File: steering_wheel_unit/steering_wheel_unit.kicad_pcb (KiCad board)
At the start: 2 copper layers, 90 x 70 mm, 130 parts, among them IC2 LM76202QPWPRQ1, J1 MAIN_CONNECTOR, J10 MODE2_SOCKET, J11 FUEL_CELL_SOCKET, J12 USB_C_Vertical, J13 Additional goldpins, J14 LCD_SOCKET, J15 JTAG_SOCKET, J16 Additional goldpins from MCU, J3 HALF_GAS_SOCKET, J4 MODE1_SOCKET, J5 FULL_GAS_SOCKET, J6 SPEED_RESET_SOCKET, J7 HORN_SOCKET, J8 SC_CLOSE_SOCKET, J9 SUPPLY_SOCKET, SW1 TL3305BF100QG, SW2 TL3305BF100QG, SW3 TL3305BF100QG, U1 STM32G491CCTx, U2 USBLC6-2P6, U3 SN65HVD232, U4 TPS62933, X1 32k768, X2 24M

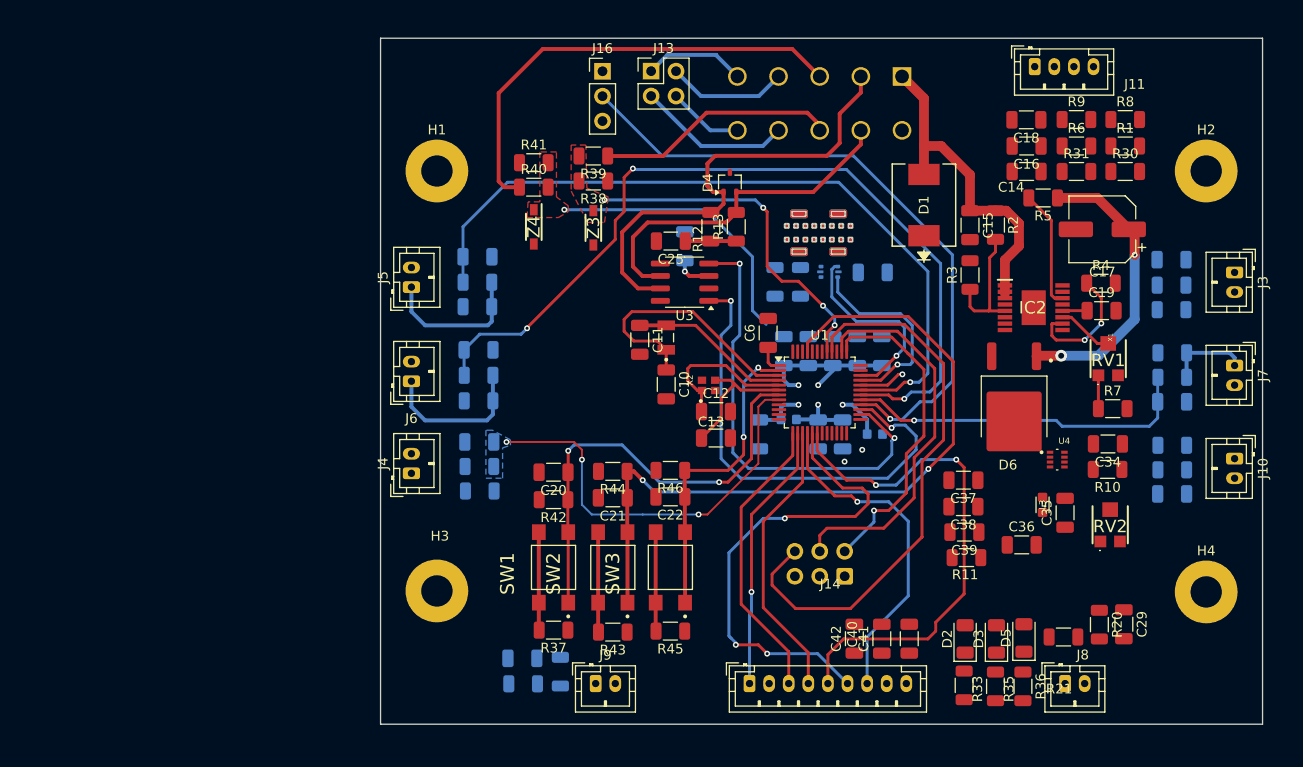
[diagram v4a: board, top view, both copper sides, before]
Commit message: Add zones for gnd and power
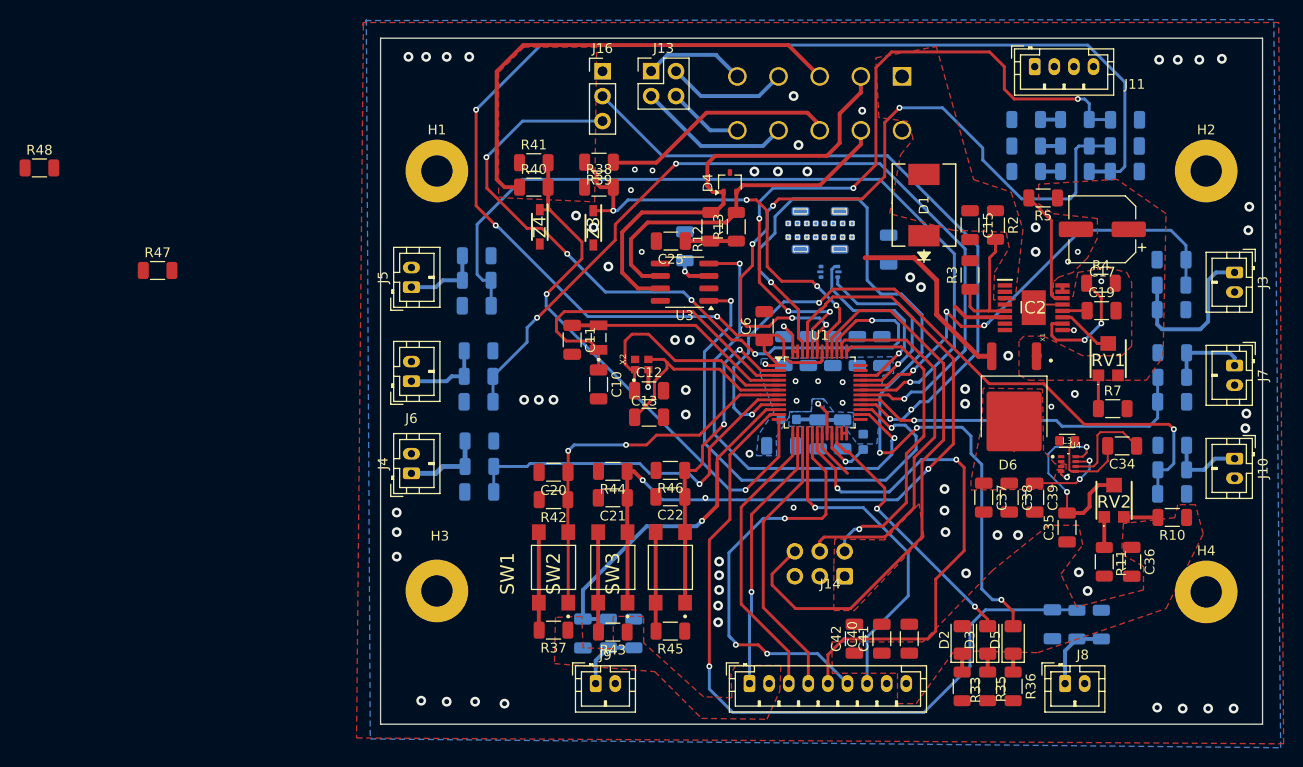
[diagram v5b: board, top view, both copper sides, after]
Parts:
- removed J12: USB_C_Vertical, Lib:CUI_UJ20-C-V-C-3-SMT-TR
- removed R32, R34: 5K1, Resistor_SMD:R_1206_3216Metric
- added J2: UJ20-C-V-C-3-SMT-TR, Lib:CUI_UJ20-C-V-C-2-SMT-TR, B.Cu at (186.7, 96.2)
- added R47: 5K1, Resistor_SMD:R_1206_3216Metric, F.Cu at (119.1, 100.3)
- added R48: 5K1, Resistor_SMD:R_1206_3216Metric, F.Cu at (107.0, 89.8)
- C14, C16, C18, C29, R1, R20, R21, R30, R31, R6, R8, R9: moved to B.Cu
- moved R11 14.1 mm to (215.7, 130.0), turned to -90 degrees
- moved C36 11.4 mm to (218.5, 130.0), turned to -90 degrees
- moved R1 10.1 mm to (207.7, 87.6), turned to 180 degrees
- moved R30 10.1 mm to (207.7, 90.2), turned to 180 degrees
- moved R8 10.1 mm to (207.7, 84.9), turned to 180 degrees
- moved R23 10.1 mm to (165.1, 137.3), turned to -90 degrees
- moved C18 10.1 mm to (217.8, 84.9), turned to 0 degrees
- moved C14 10.0 mm to (217.8, 90.2), turned to 0 degrees
- moved C16 10.0 mm to (217.8, 87.6), turned to 0 degrees
- moved R27 8.45 mm to (167.7, 137.3)
- moved R10 8.22 mm to (222.6, 125.5)
- moved C39 7.99 mm to (208.6, 123.5), turned to -90 degrees
- moved C29 7.29 mm to (210.4, 136.4)
- moved C12 7.15 mm to (169.3, 112.6)
- moved C13 7.15 mm to (169.3, 115.3)
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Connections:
- net Net-(U1-VREF+) renamed /MCU/VREF
- net Net-(U4-VIN) renamed /POWER/VIN
- U1 pad 22: /MCU/MCU_LED -> /IO/MCU_LED
- U1 pad 46: /MCU/CAN_LED -> /IO/CAN_LED
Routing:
- net /IO/FUEL_CELL_RACE_BUTTON_MCU: track 0.00 -> 136.6 mm, vias 0 -> 3
- net /IO/CAN_LED: track 0.00 -> 89.6 mm, vias 0 -> 4
- net /IO/FUEL_CELL_PREPARE_TO_RAC_BUTTON_MCU: track 0.00 -> 77.4 mm, vias 0 -> 5
- net /IO/SC_CLOSE_BUTTON_MCU: track 0.00 -> 76.8 mm, vias 0 -> 1
- net /MCU/GPIO_PB15: track 0.00 -> 76.3 mm, vias 0 -> 5
- net /IO/FUEL_CELL_OFF_BUTTON_MCU: track 0.00 -> 74.7 mm, vias 0 -> 5
- net /IO/MODE2_BUTTON_MCU: track 0.00 -> 72.5 mm, vias 0 -> 3
- net /IO/HALF_GAS_BUTTON_MCU: track 4.73 -> 47.9 mm, vias 1 -> 3
- net /IO/SUPPLY_BUTTON_MCU: track 0.00 -> 36.0 mm, vias 0 -> 1
- net +12V: track 33.9 -> 0.16 mm
- net /POWER/Vreg: track 29.6 -> 0.72 mm, vias 2 -> 0
- net /IO/MCU_LED: track 0.00 -> 26.9 mm, vias 0 -> 2
- net /MCU/PA4: track 28.7 -> 55.3 mm, vias 1 -> 2
- net GND: track 0.00 -> 21.9 mm, vias 2 -> 74
- net Net-(U4-FB): track 0.00 -> 19.7 mm, vias 0 -> 2
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- added copper zone on F.Cu, net +12V
- added copper zone on B.Cu, net +3.3V
- added copper zone on F.Cu, net +3.3V
- added copper zone on B.Cu, net /MCU/VREF
- added copper zone on F.Cu, net /POWER/VIN
- added copper zone on F.Cu, net /POWER/Vreg
- added copper zone on B.Cu, net GND
- added copper zone on F.Cu, net GND
- removed copper zone on B.Cu, net /IO/MODE1_BUTTON_MCU
- removed copper zone on F.Cu, net /MCU/PA4
- removed copper zone on F.Cu, net /MCU/PB4

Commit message: Add some routing changes
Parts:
- R47, R48: moved to B.Cu
- moved R48 87.1 mm to (193.5, 100.1), turned to -90 degrees
- moved R47 77.1 mm to (196.2, 100.1), turned to -90 degrees
- moved C23 18.0 mm to (175.7, 97.9), turned to 90 degrees
- moved C18 16.9 mm to (200.9, 84.1), turned to -90 degrees
- moved R9 9.21 mm to (203.5, 84.1), turned to 90 degrees
- moved R1 9.05 mm to (216.2, 84.3), turned to -90 degrees
- moved C16 7.62 mm to (210.9, 84.3), turned to -90 degrees
- moved C26 5.40 mm to (222.7, 104.6), turned to 0 degrees
- moved R14 4.60 mm to (222.7, 99.7), turned to 180 degrees
- moved R6 3.39 mm to (213.6, 84.3), turned to -90 degrees
- moved R30 3.02 mm to (210.8, 90.3), turned to -90 degrees
- moved U2 2.92 mm to (184.7, 100.5), turned to 180 degrees
- moved R8 1.78 mm to (206.1, 84.1), turned to -90 degrees
- moved C14 1.59 mm to (216.2, 90.3), turned to -90 degrees
- moved C34 0.90 mm to (217.5, 119.1)
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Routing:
- net +3.3V: track 8.71 -> 300.3 mm, vias 7 -> 16
- net /FUEL_CELL_RACE_MODE: track 2.05 -> 26.9 mm
- net /IO/FUEL_CELL_OFF_BUTTON_MCU: track 74.7 -> 62.6 mm
- net /HALF_GAS: track 17.0 -> 7.67 mm
- net /FUEL_CELL_PREPARE_TO_RACE: track 2.05 -> 11.3 mm
- net /FUEL_CELL_OFF: track 2.05 -> 9.64 mm
- net /IO/HALF_GAS_BUTTON_MCU: track 47.9 -> 40.4 mm
- net /LCD_CS: track 34.4 -> 40.9 mm, vias 1 -> 3
- net /IO/FUEL_CELL_RACE_BUTTON_MCU: track 136.6 -> 142.9 mm
- net /MCU/PA4: track 55.3 -> 61.6 mm
- net /MCU/USB_DN: track 19.7 -> 25.1 mm
- net /IO/FUEL_CELL_PREPARE_TO_RAC_BUTTON_MCU: track 77.4 -> 73.2 mm
- net /IO/FULL_GAS_BUTTON_MCU: track 84.0 -> 86.7 mm
- net /IO/MODE2_BUTTON_MCU: track 72.5 -> 75.0 mm
- net /SC_CLOSE: track 7.54 -> 10.0 mm
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
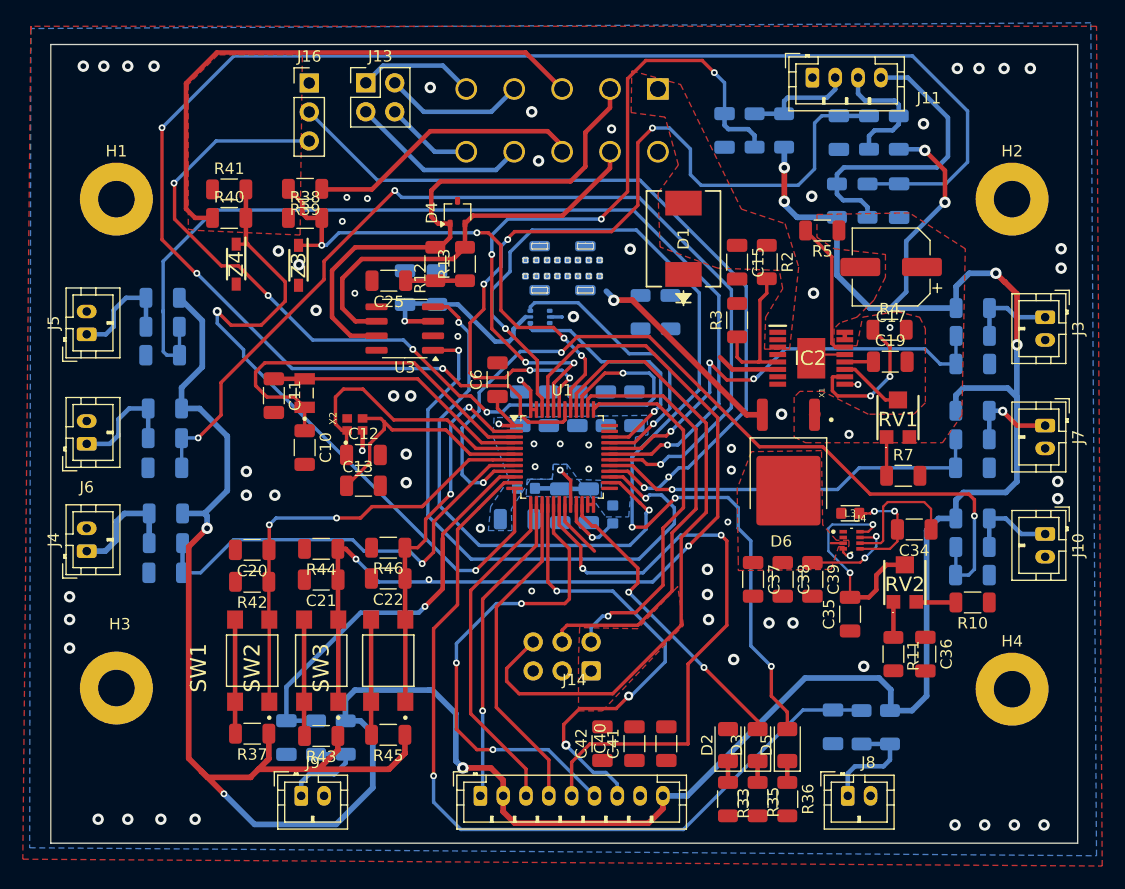
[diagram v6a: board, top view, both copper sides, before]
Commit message: Edit tracks and add captions of elements
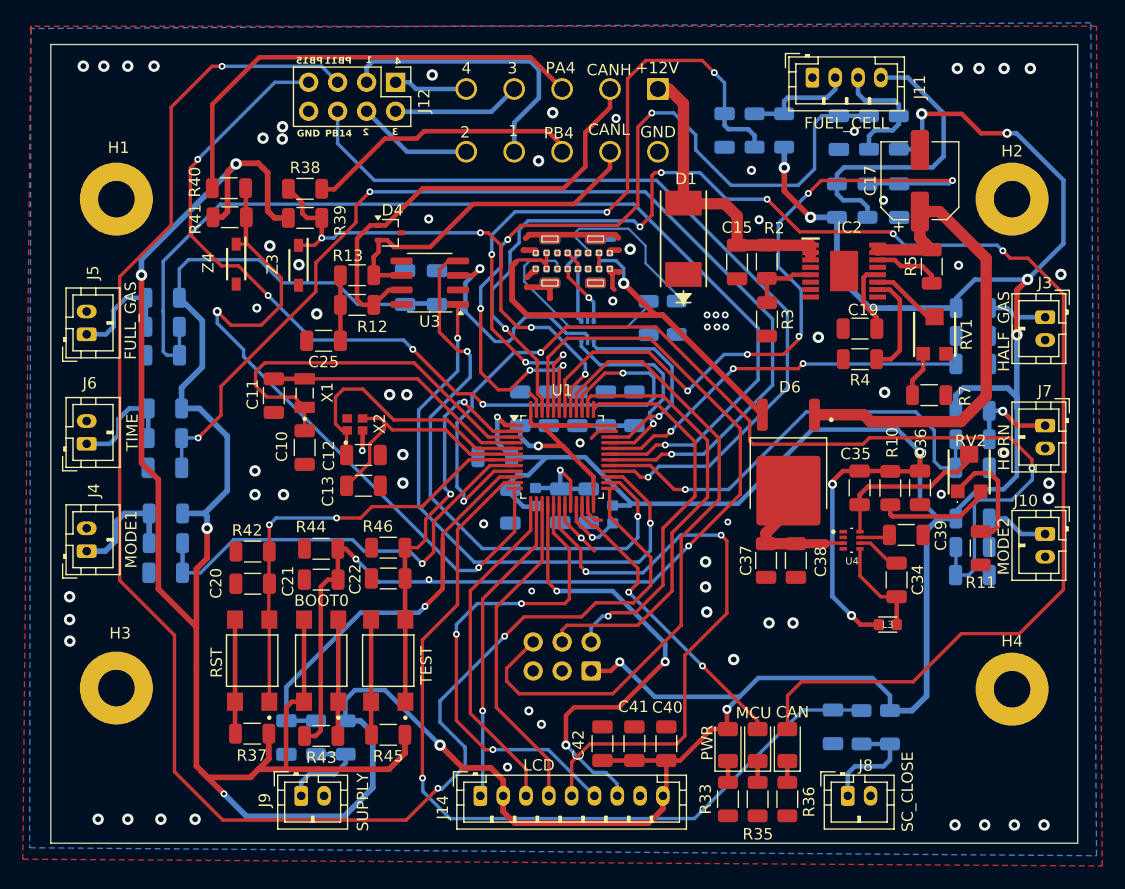
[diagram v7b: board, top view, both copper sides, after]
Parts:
- removed J13: Additional goldpins, Connector_PinHeader_2.54mm:PinHeader_2x02_P2.54mm_Vertical
- removed J16: Additional goldpins from MCU, Connector_PinHeader_2.54mm:PinHeader_1x03_P2.54mm_Vertical
- added J12: Additional goldpins, Connector_PinHeader_2.54mm:PinHeader_2x04_P2.54mm_Vertical, F.Cu at (172.1, 79.9)
- C6: moved to B.Cu
- J10: value MODE2_SOCKET -> MODE2
- J11: value FUEL_CELL_SOCKET -> FUEL_CELL
- J14: value LCD_SOCKET -> LCD
- J2: footprint Lib:CUI_UJ20-C-V-C-2-SMT-TR -> Lib:CUI_UJ20-C-V-C-3-SMT-TR
- J3: value HALF_GAS_SOCKET -> HALF_GAS
- J4: value MODE1_SOCKET -> MODE1
- J5: value FULL_GAS_SOCKET -> FULL_GAS
- J6: value SPEED_RESET_SOCKET -> TIME
- J7: value HORN_SOCKET -> HORN
- J8: value SC_CLOSE_SOCKET -> SC_CLOSE
- J9: value SUPPLY_SOCKET -> SUPPLY
- moved C36 14.6 mm to (218.0, 115.5)
- moved R10 12.4 mm to (215.4, 115.5), turned to -90 degrees
- moved R11 12.0 mm to (223.3, 120.7)
- moved RV2 11.2 mm to (222.3, 114.1)
- moved C35 11.1 mm to (212.7, 115.5), turned to -90 degrees
- moved L3 10.3 mm to (215.2, 127.4)
- moved R5 10.1 mm to (219.1, 96.1), turned to -90 degrees
- moved R13 9.50 mm to (168.7, 96.8), turned to 0 degrees
- moved C39 9.10 mm to (216.8, 119.6), turned to 0 degrees
- moved IC2 8.17 mm to (211.4, 96.5)
- moved C17 7.97 mm to (218.0, 88.5), turned to 90 degrees
- moved RV1 7.97 mm to (219.3, 102.0)
- moved C25 7.78 mm to (165.8, 102.6)
- moved R12 7.73 mm to (168.7, 99.4), turned to 0 degrees
- moved R7 7.43 mm to (218.8, 107.3)
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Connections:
- net Net-(U1-VDDA) renamed /MCU/VDDA
- R43 pad 1: +3.3V -> Net-(R43-Pad1)
- R43 pad 2: Net-(SW2-A) -> /MCU/BOOT0
- SW2 pad 1: /MCU/BOOT0 -> Net-(R43-Pad1)
- SW2 pad 2: /MCU/BOOT0 -> Net-(R43-Pad1)
- SW2 pad 3: Net-(SW2-A) -> +3.3V
- SW2 pad 4: Net-(SW2-A) -> +3.3V
- U1 pad 24: GND -> +3.3V
- U1 pad 25: /MCU/GPIO_PB11 -> /PB11
- U1 pad 28: /MCU/GPIO_PB14 -> /PB14
- U1 pad 36: GND -> +3.3V
- U1 pad 39: /MCU/GPIO_PB15 -> /PB15
- U1 pad 48: GND -> +3.3V
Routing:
- net +3.3V: track 300.3 -> 552.2 mm, vias 16 -> 19
- net /PB11: track 0.00 -> 147.3 mm, vias 0 -> 3
- net /IO/FUEL_CELL_RACE_BUTTON_MCU: track 142.9 -> 62.8 mm, vias 3 -> 5
- net /PB15: track 0.00 -> 76.7 mm, vias 0 -> 5
- net /MCU/GPIO_PB15: track 76.3 -> 0.00 mm, vias 5 -> 0
- net /PB14: track 0.00 -> 74.1 mm, vias 0 -> 1
- net /MCU/GPIO_PB14: track 70.9 -> 0.00 mm, vias 2 -> 0
- net /POWER/Vreg: track 0.72 -> 44.5 mm
- net /IO/CAN_LED: track 90.9 -> 132.1 mm, vias 4 -> 6
- net +12V: track 0.16 -> 26.6 mm
- net /VBUS: track 18.3 -> 42.2 mm
- net Net-(J2-CC2-PadB5_1): track 0.00 -> 19.0 mm
- net /IO/MODE2_BUTTON_MCU: track 75.0 -> 91.3 mm
- net Net-(J2-CC1-PadA5_1): track 0.00 -> 14.9 mm
- net /POWER/VIN: track 1.10 -> 12.4 mm
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- removed copper zone on F.Cu, net +12V
- removed copper zone on B.Cu, net +3.3V
- removed copper zone on F.Cu, net +3.3V
- removed copper zone on B.Cu, net /MCU/VREF
- removed copper zone on F.Cu, net /POWER/VIN
- removed copper zone on F.Cu, net /POWER/Vreg
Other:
- board text added: "+12V"
- board text added: "1"
- board text added: "2"
- board text added: "3"
- board text added: "4"
- board text added: "BOOT0"
- board text added: "CAN"
- board text added: "CANH"
- board text added: "CANL"
- board text added: "GND"
- board text added: "MCU"
- board text added: "PA4"
- board text added: "PB11"
- board text added: "PB14"
- board text added: "PB15"
- board text added: "PB4"
- board text added: "PWR"
- board text added: "RST"
- board text added: "TEST"

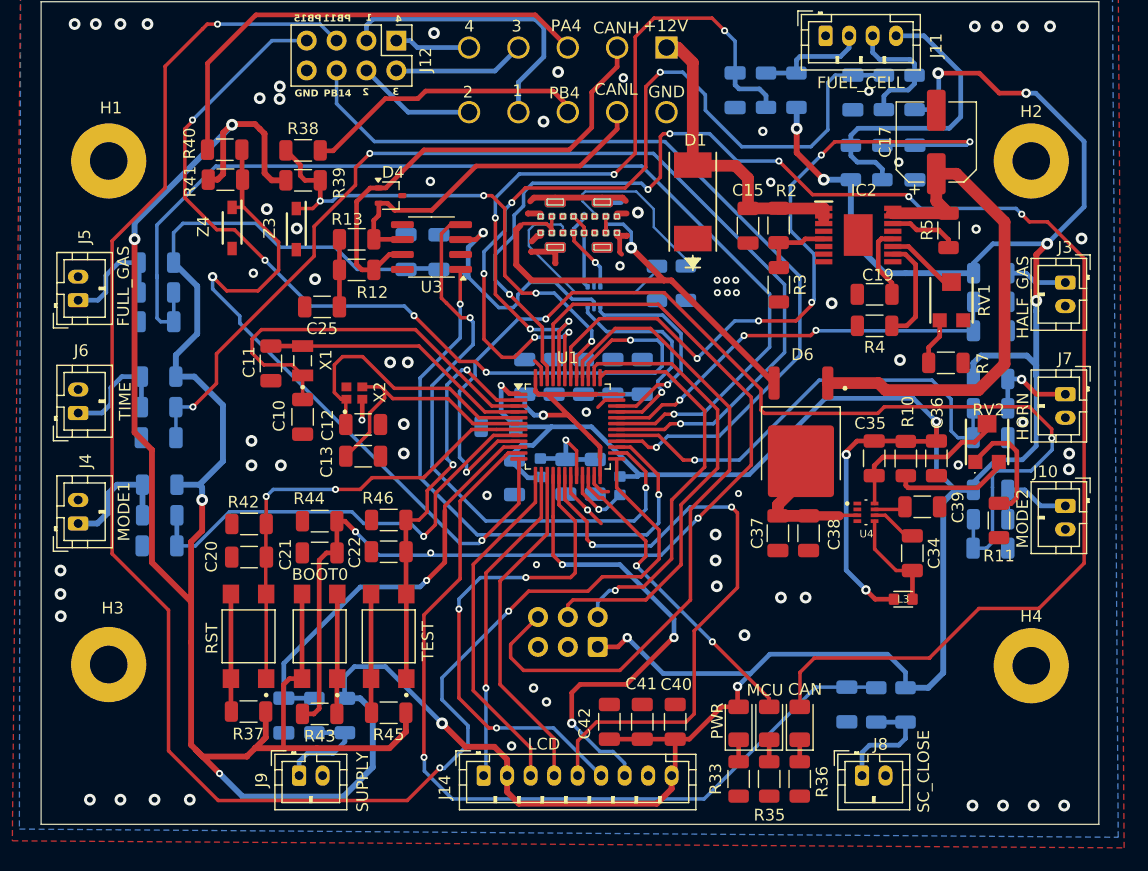
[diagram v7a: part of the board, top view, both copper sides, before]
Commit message: Add dimensions
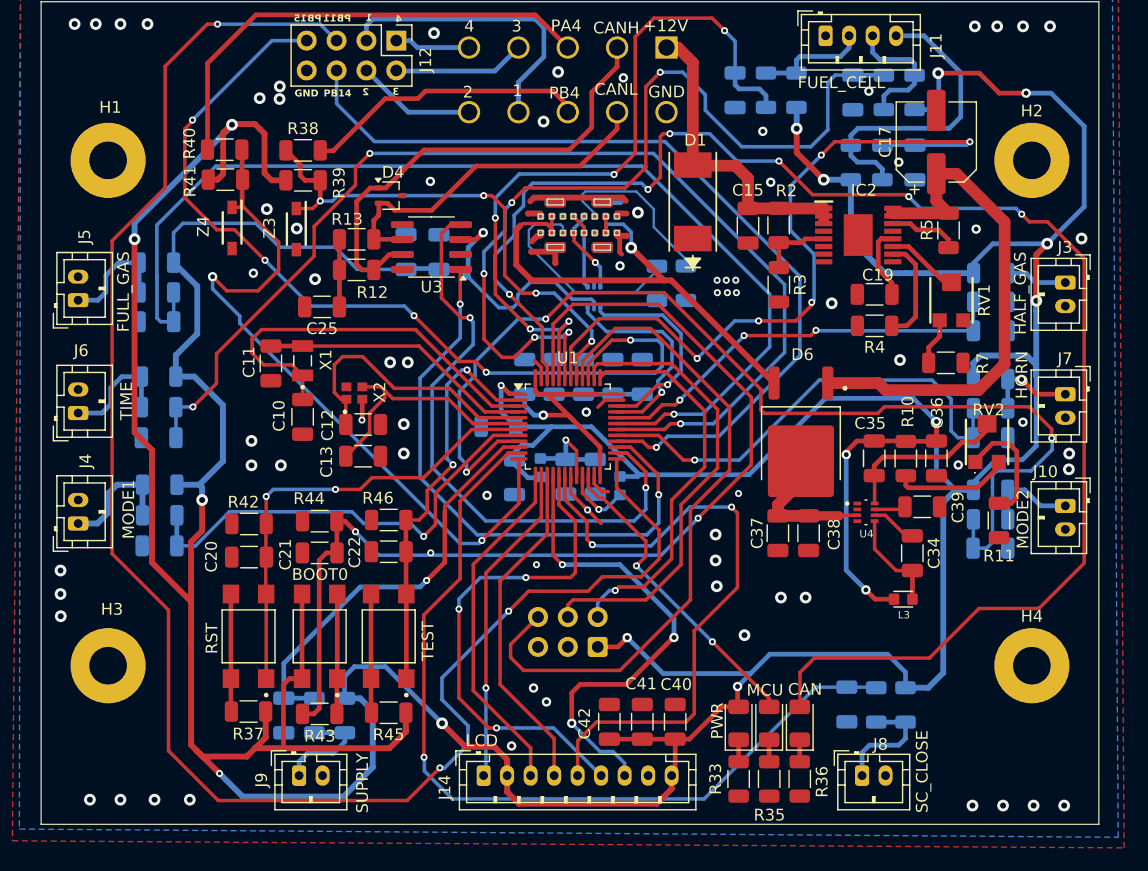
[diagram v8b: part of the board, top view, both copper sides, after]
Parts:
- J10: value MODE2 -> MODE2_SOCKET
- J11: value FUEL_CELL -> FUEL_CELL_SOCKET
- J14: value LCD -> LCD_SOCKET
- J3: value HALF_GAS -> HALF_GAS_SOCKET
- J4: value MODE1 -> MODE1_SOCKET
- J5: value FULL_GAS -> FULL_GAS_SOCKET
- J6: value TIME -> SPEED_RESET_SOCKET
- J7: value HORN -> HORN_SOCKET
- J8: value SC_CLOSE -> SC_CLOSE_SOCKET
- J9: value SUPPLY -> SUPPLY_SOCKET
- moved H3 0.11 mm to (147.6, 133.1)
- moved H2 0.07 mm to (226.2, 90.1)
- moved H1 0.07 mm to (147.6, 90.1)
- moved H4 0.05 mm to (226.2, 133.1)
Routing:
- net +3.3V: track 552.2 -> 552.9 mm
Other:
- board text added: "FUEL_CELL"
- board text added: "FULL_GAS"
- board text added: "HALF_GAS"
- board text added: "HORN"
- board text added: "LCD"
- board text added: "MODE1"
- board text added: "MODE2"
- board text added: "SC_CLOSE"
- board text added: "SUPPLY"
- board text added: "TIME"
